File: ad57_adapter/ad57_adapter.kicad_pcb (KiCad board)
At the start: 2 copper layers, 60 x 60 mm, 11 parts, among them J1 Screw_Terminal_01x02, J10 615008140421, J11 615008140421, J3 Screw_Terminal_01x06, J4 Screw_Terminal_01x06, J5 180-015-213R911, J6 180-015-213R911, J7 615008140421, J8 Screw_Terminal_01x06, J9 615008140421

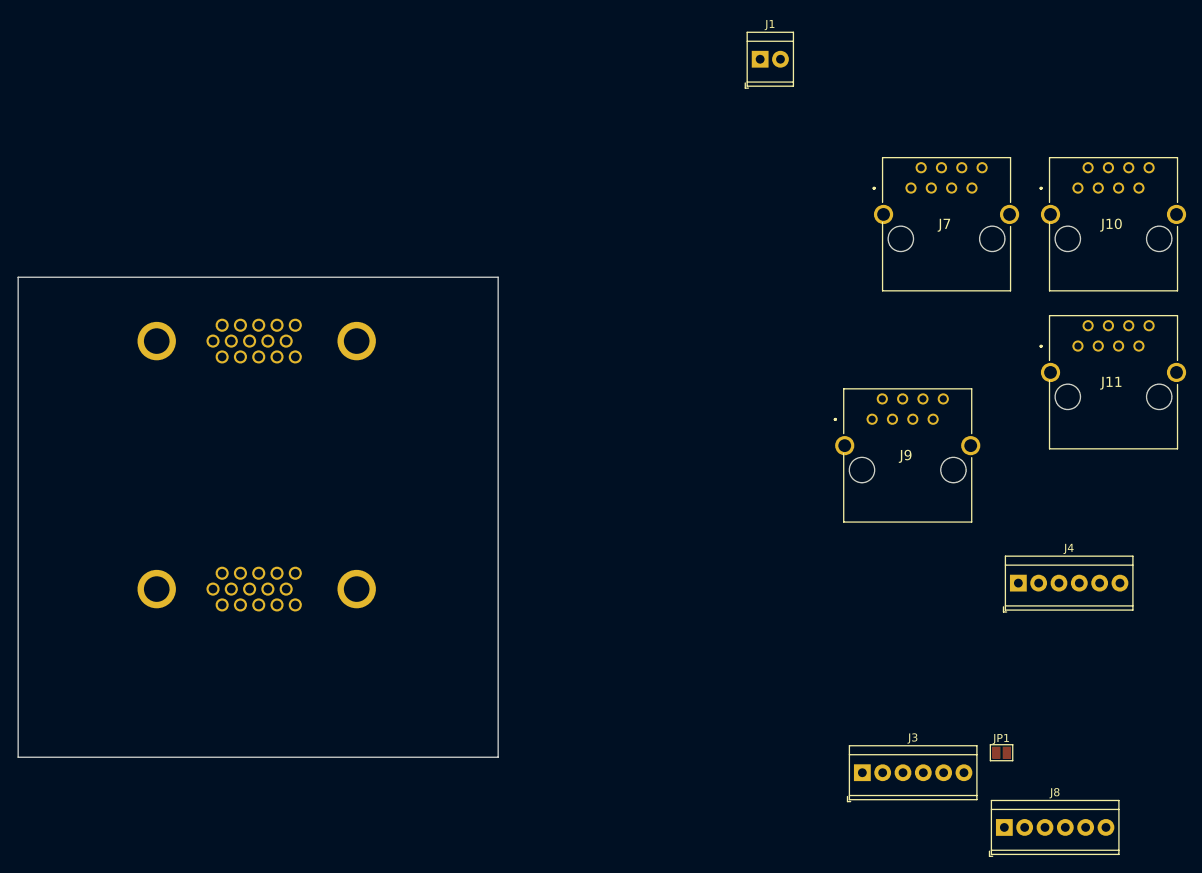
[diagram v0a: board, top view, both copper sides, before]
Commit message: connectors arranged. outline drawn
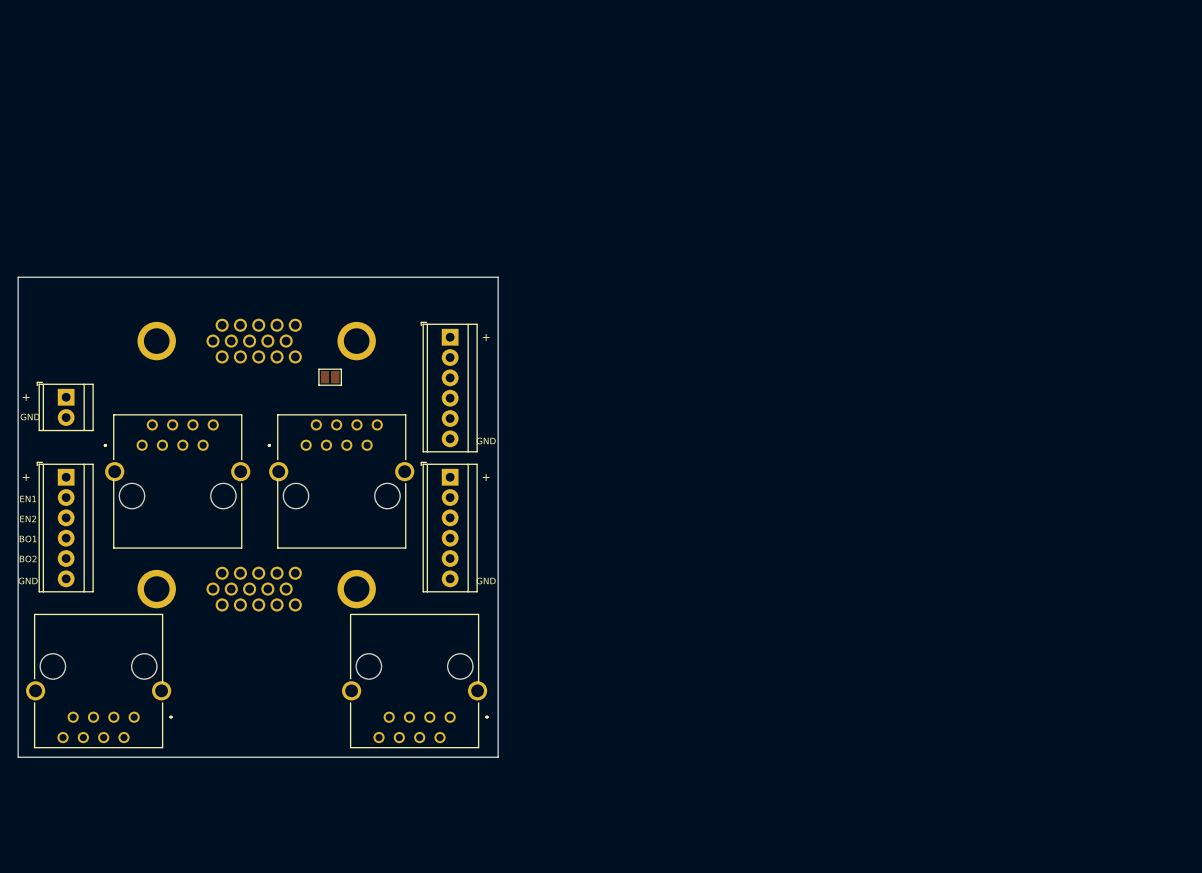
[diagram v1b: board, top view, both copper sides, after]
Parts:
- moved J8 125.2 mm to (130.5, 88.0), turned to 270 degrees
- moved J7 117.5 mm to (139.0, 118.0), turned to 180 degrees
- moved J10 102.6 mm to (178.5, 118.0), turned to 180 degrees
- moved J11 97.3 mm to (160.5, 84.0)
- moved J1 96.5 mm to (130.5, 78.0), turned to 270 degrees
- moved JP1 96.2 mm to (163.5, 75.5), turned to 180 degrees
- moved J9 91.3 mm to (140.0, 84.0)
- moved J3 75.0 mm to (178.5, 70.5), turned to 270 degrees
- moved J4 72.2 mm to (178.5, 88.0), turned to 270 degrees
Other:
- board text added: "+"
- board text added: "BO1"
- board text added: "BO2"
- board text added: "EN1"
- board text added: "EN2"
- board text added: "GND"

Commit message: finished routing.
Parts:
- moved JP1 18.9 mm to (144.6, 75.8), turned to 0 degrees
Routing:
- net RXD1: track 0.00 -> 83.8 mm, vias 0 -> 1
- net TXD1: track 0.00 -> 76.3 mm, vias 0 -> 1
- net BZZOUT1: track 0.00 -> 70.0 mm, vias 0 -> 1
- net USENS2: track 0.00 -> 67.1 mm
- net TXD2: track 0.00 -> 57.0 mm
- net EN1: track 0.00 -> 53.8 mm
- net DIN2: track 0.00 -> 52.7 mm
- net RXD2: track 0.00 -> 44.3 mm, vias 0 -> 2
- net USENS1: track 0.00 -> 42.1 mm
- net CANHI: track 0.00 -> 41.9 mm
- net CANLO: track 0.00 -> 40.0 mm, vias 0 -> 1
- net DOUT1: track 0.00 -> 39.7 mm, vias 0 -> 1
- net DOUT2: track 0.00 -> 38.8 mm, vias 0 -> 2
- net BZZOUT2: track 0.00 -> 33.5 mm
- net EN2: track 0.00 -> 29.3 mm
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- added copper zone on In1.Cu, net GND
- added copper zone on In2.Cu, net VIN
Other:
- copper layers 2 -> 4
- board text added: "AD57 Adapter"
- board text added: "Close for CAN Termination"
- board text added: "DI1"
- board text added: "DI2"
- board text added: "DO1"
- board text added: "DO2"
- board text added: "DO3"
- board text added: "DO4"
- board text added: "Maximilian Betz"
- board text added: "US1"
- board text added: "US2"
- board text added: "V1.0 2021-02-11"
- board text added: "pcbDesign:"

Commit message: generated gerber. Schematic PDF export,  3D-View immages.
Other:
- outline, holes or cut-outs redrawn
- board text added: "AD57 Bottom Connector"
- board text added: "AD57 Top Connector"
- board text added: "CAN"
- board text added: "RS231_1"
- board text added: "RS232_2"
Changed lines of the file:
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@@
   (general
     (thickness 1.6)
-    (drawings 29)
+    (drawings 39)
     (tracks 162)
     (zones 0)
@@
   )
   (page A4)
+  (title_block
+    (title "AD57 Adapter PCB")
+    (date 2021-02-10)
+    (rev 1.0)
+    (comment 4 "Maximilian Betz")
+  )
   (layers
     (0 F.Cu signal)
@@
       (psa4output false)
       (plotreference true)
-      (plotvalue true)
+      (plotvalue false)
       (plotinvisibletext false)
-      (padsonsilk false)
+      (padsonsilk true)
       (subtractmaskfromsilk false)
       (outputformat 1)
       (mirror false)
-      (drillshape 1)
+      (drillshape 0)
       (scaleselection 1)
-      (outputdirectory ""))
+      (outputdirectory "gerber{"))
   )
   (net 0 "")
@@
       (net 21 CANLO))
   )
-  (gr_text "Close for CAN \nTermination" (at 152 76.25) (layer F.SilkS)
-    (effects (font (size 1 1) (thickness 0.15)))
-  )
-  (gr_text "V1.0 2021-02-11" (at 131.5 72.5) (layer F.SilkS)
-    (effects (font (size 0.8 0.8) (thickness 0.1)))
-  )
-  (gr_text "AD57 \nAdapter" (at 130.25 68.75) (layer F.SilkS)
+  (gr_arc (start 182 120.5) (end 182 123) (angle -90) (layer Edge.Cuts) (width 0.05))
+  (gr_arc (start 127 120.5) (end 124.5 120.5) (angle -90) (layer Edge.Cuts) (width 0.05))
+  (gr_arc (start 127 65.5) (end 127 63) (angle -90) (layer Edge.Cuts) (width 0.05))
+  (gr_arc (start 182 65.5) (end 184.5 65.5) (angle -90) (layer Edge.Cuts) (width 0.05))
+  (gr_text CAN (at 138.75 78.75) (layer F.SilkS)
+    (effects (font (size 1.5 1.5) (thickness 0.2)))
+  )
+  (gr_text "AD57 Bottom\nConnector" (at 132.5 104.75) (layer B.SilkS)
+    (effects (font (size 1 1) (thickness 0.15)) (justify mirror))
+  )
+  (gr_text "AD57 Top \nConnector" (at 174.75 66.25) (layer B.SilkS)
+    (effects (font (size 1 1) (thickness 0.15)) (justify mirror))
+  )
+  (gr_text CAN (at 159.25 78.75) (layer F.SilkS)
+    (effects (font (size 1.5 1.5) (thickness 0.2)))
+  )
+  (gr_text RS232_2 (at 164 110 90) (layer F.SilkS)
+    (effects (font (size 1.5 1.5) (thickness 0.2)))
+  )
+  (gr_text RS231_1 (at 145 110 90) (layer F.SilkS)
+    (effects (font (size 1.5 1.5) (thickness 0.2)))
+  )
+  (gr_text "Close for CAN Termination" (at 154.5 75.75) (layer F.SilkS)
+    (effects (font (size 0.8 0.8) (thickness 0.1)))
+  )
+  (gr_text "V1.0 2021-02-11" (at 131.5 71) (layer F.SilkS)
+    (effects (font (size 0.8 0.8) (thickness 0.1)))
+  )
+  (gr_text "AD57 \nAdapter" (at 130.25 67) (layer F.SilkS)
     (effects (font (size 1.5 1.5) (thickness 0.2)))
   )
@@
     (effects (font (size 1 1) (thickness 0.15)))
   )
-  (gr_line (start 124.5 123) (end 124.5 63) (layer Edge.Cuts) (width 0.05))
-  (gr_line (start 184.5 123) (end 124.5 123) (layer Edge.Cuts) (width 0.05))
-  (gr_line (start 184.5 63) (end 184.5 123) (layer Edge.Cuts) (width 0.05))
-  (gr_line (start 124.5 63) (end 184.5 63) (layer Edge.Cuts) (width 0.05))
+  (gr_line (start 124.5 120.5) (end 124.5 65.5) (layer Edge.Cuts) (width 0.05))
+  (gr_line (start 182 123) (end 127 123) (layer Edge.Cuts) (width 0.05))
+  (gr_line (start 184.5 65.5) (end 184.5 120.5) (layer Edge.Cuts) (width 0.05))
+  (gr_line (start 127 63) (end 182 63) (layer Edge.Cuts) (width 0.05))
   (segment (start 150 72.962) (end 148.212 72.962) (width 0.3) (layer B.Cu) (net 3))
   (segment (start 148.212 72.962) (end 146.75 71.5) (width 0.3) (layer B.Cu) (net 3))
